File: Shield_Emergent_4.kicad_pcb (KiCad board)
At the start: 4 copper layers, 27 x 36 mm, 32 parts, among them J1 TF31-18S-0.5SH_800_, J2 Conn_01x04_Socket, J3 TF31-18S-0.5SH_800_, J5 Conn_01x02_Socket, J6 Conn_01x02_Socket, U3 SP3012-06UTG, U4 SP3012-06UTG, X1 USB_C_24pins

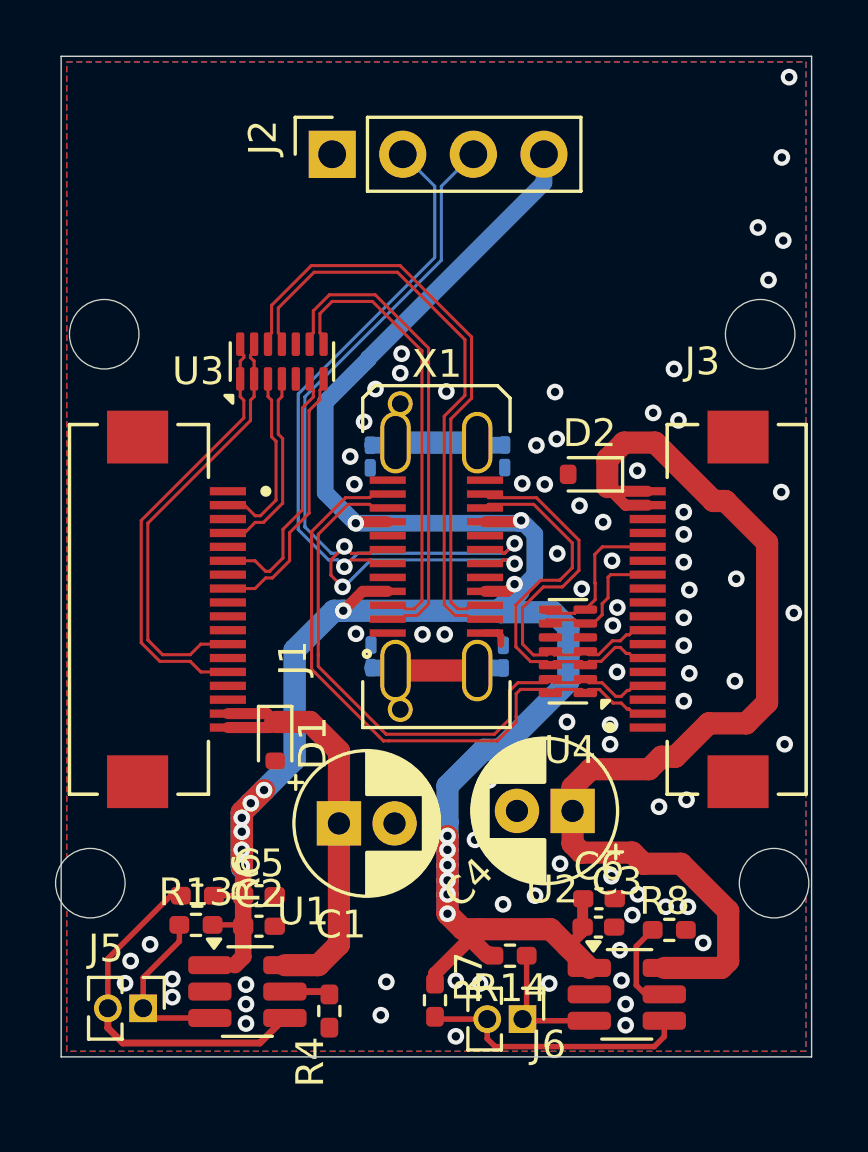
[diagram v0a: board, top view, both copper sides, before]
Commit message: v0.2 silkscreen was corrected, DRC was completed
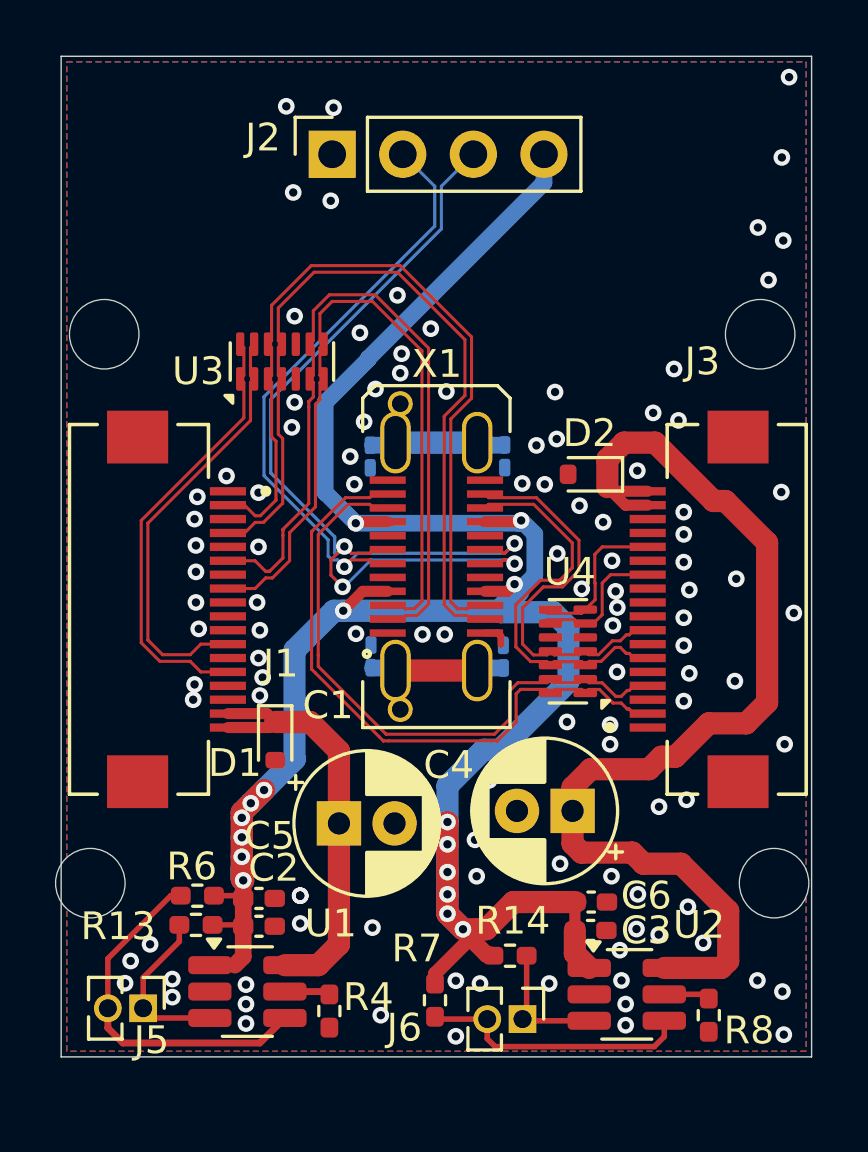
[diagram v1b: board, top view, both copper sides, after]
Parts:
- moved R8 3.38 mm to (23.3, 34.5), turned to -90 degrees
- moved C6 0.30 mm to (19.1, 30.4)
- moved C3 0.30 mm to (19.1, 31.4)
- moved C5 0.10 mm to (7.12, 30.3)
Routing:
- net VBUS: track 87.3 -> 89.6 mm
- net TX1-: track 25.8 -> 27.2 mm
- net RX1-: track 28.1 -> 29.5 mm
- net RX1+: track 28.1 -> 29.5 mm
- net TX1+: track 26.6 -> 28.0 mm
- net Net-(U2-ILIM): track 3.38 -> 2.34 mm
- net D+: track 27.7 -> 28.6 mm
- net D-: track 29.2 -> 30.1 mm
- net GND: vias 82 -> 118
